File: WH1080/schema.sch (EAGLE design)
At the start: 18 parts

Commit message: +
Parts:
- removed ANEMO, RAIN: XRJK-S-01-6-4-0-9M2, con-xmultiple:XRJK-S-01-6-4-0-9M2
- added J1, J2: RJ11, SparkFun-Connectors:RJ11-6
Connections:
- net GND: now also J1.3, J2.2, J2.3; no longer ANEMO.1, ANEMO.2, RAIN.2
- net N$1: now also J1.4; no longer RAIN.3
- net N$2: now also J2.5; no longer ANEMO.4
- net N$4: now also J2.4; no longer ANEMO.3

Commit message: +
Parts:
- removed J1, J2: RJ11, SparkFun-Connectors:RJ11-6
- added RAIN, WIND: RJ11-4, pf:RJ11-4
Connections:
- net GND: now also RAIN.3, WIND.2, WIND.4; no longer J1.3, J2.2, J2.3
- net N$1: now also RAIN.4; no longer J1.4
- net N$2: now also WIND.5; no longer J2.5
- net N$4: now also WIND.3; no longer J2.4
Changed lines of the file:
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@@
 <grid distance="0.1" unitdist="inch" unit="inch" style="lines" multiple="1" display="no" altdistance="0.01" altunitdist="inch" altunit="inch"/>
 <layers>
-<layer number="1" name="Top" color="4" fill="1" visible="yes" active="no"/>
-<layer number="16" name="Bottom" color="1" fill="1" visible="yes" active="no"/>
-<layer number="17" name="Pads" color="2" fill="1" visible="yes" active="no"/>
-<layer number="18" name="Vias" color="2" fill="1" visible="yes" active="no"/>
-<layer number="19" name="Unrouted" color="6" fill="1" visible="yes" active="no"/>
-<layer number="20" name="Dimension" color="24" fill="1" visible="yes" active="no"/>
-<layer number="21" name="tPlace" color="7" fill="1" visible="yes" active="no"/>
-<layer number="22" name="bPlace" color="7" fill="1" visible="yes" active="no"/>
-<layer number="23" name="tOrigins" color="15" fill="1" visible="yes" active="no"/>
-<layer number="24" name="bOrigins" color="15" fill="1" visible="yes" active="no"/>
-<layer number="25" name="tNames" color="7" fill="1" visible="yes" active="no"/>
-<layer number="26" name="bNames" color="7" fill="1" visible="yes" active="no"/>
-<layer number="27" name="tValues" color="7" fill="1" visible="yes" active="no"/>
-<layer number="28" name="bValues" color="7" fill="1" visible="yes" active="no"/>
+<layer number="1" name="Top" color="4" fill="1" visible="no" active="no"/>
+<layer number="16" name="Bottom" color="1" fill="1" visible="no" active="no"/>
+<layer number="17" name="Pads" color="2" fill="1" visible="no" active="no"/>
+<layer number="18" name="Vias" color="2" fill="1" visible="no" active="no"/>
+<layer number="19" name="Unrouted" color="6" fill="1" visible="no" active="no"/>
+<layer number="20" name="Dimension" color="24" fill="1" visible="no" active="no"/>
+<layer number="21" name="tPlace" color="7" fill="1" visible="no" active="no"/>
+<layer number="22" name="bPlace" color="7" fill="1" visible="no" active="no"/>
+<layer number="23" name="tOrigins" color="15" fill="1" visible="no" active="no"/>
+<layer number="24" name="bOrigins" color="15" fill="1" visible="no" active="no"/>
+<layer number="25" name="tNames" color="7" fill="1" visible="no" active="no"/>
+<layer number="26" name="bNames" color="7" fill="1" visible="no" active="no"/>
+<layer number="27" name="tValues" color="7" fill="1" visible="no" active="no"/>
+<layer number="28" name="bValues" color="7" fill="1" visible="no" active="no"/>
 <layer number="29" name="tStop" color="7" fill="3" visible="no" active="no"/>
 <layer number="30" name="bStop" color="7" fill="6" visible="no" active="no"/>
@@
 <layer number="35" name="tGlue" color="7" fill="4" visible="no" active="no"/>
 <layer number="36" name="bGlue" color="7" fill="5" visible="no" active="no"/>
-<layer number="37" name="tTest" color="7" fill="1" visible="yes" active="no"/>
-<layer number="38" name="bTest" color="7" fill="1" visible="yes" active="no"/>
+<layer number="37" name="tTest" color="7" fill="1" visible="no" active="no"/>
+<layer number="38" name="bTest" color="7" fill="1" visible="no" active="no"/>
 <layer number="39" name="tKeepout" color="4" fill="11" visible="no" active="no"/>
 <layer number="40" name="bKeepout" color="1" fill="11" visible="no" active="no"/>
@@
 <layer number="44" name="Drills" color="7" fill="1" visible="no" active="no"/>
 <layer number="45" name="Holes" color="7" fill="1" visible="no" active="no"/>
-<layer number="46" name="Milling" color="3" fill="1" visible="yes" active="no"/>
-<layer number="47" name="Measures" color="7" fill="1" visible="yes" active="no"/>
-<layer number="48" name="Document" color="7" fill="1" visible="yes" active="no"/>
-<layer number="49" name="Reference" color="7" fill="1" visible="yes" active="no"/>
-<layer number="50" name="dxf" color="7" fill="1" visible="yes" active="no"/>
-<layer number="51" name="tDocu" color="7" fill="1" visible="yes" active="no"/>
-<layer number="52" name="bDocu" color="7" fill="1" visible="yes" active="no"/>
+<layer number="46" name="Milling" color="3" fill="1" visible="no" active="no"/>
+<layer number="47" name="Measures" color="7" fill="1" visible="no" active="no"/>
+<layer number="48" name="Document" color="7" fill="1" visible="no" active="no"/>
+<layer number="49" name="Reference" color="7" fill="1" visible="no" active="no"/>
+<layer number="50" name="dxf" color="7" fill="1" visible="no" active="no"/>
+<layer number="51" name="tDocu" color="7" fill="1" visible="no" active="no"/>
+<layer number="52" name="bDocu" color="7" fill="1" visible="no" active="no"/>
 <layer number="53" name="tGND_GNDA" color="7" fill="9" visible="no" active="no"/>
 <layer number="54" name="bGND_GNDA" color="1" fill="9" visible="no" active="no"/>
@@
 <part name="C3" library="rcl" library_urn="urn:adsk.eagle:library:334" deviceset="C-EU" device="025-024X044" package3d_urn="urn:adsk.eagle:package:23630/1" value="100n"/>
 <part name="GND9" library="supply1" library_urn="urn:adsk.eagle:library:371" deviceset="GND" device=""/>
-<part name="J1" library="SparkFun-Connectors" deviceset="RJ11-6" device="" value="RJ11"/>
-<part name="J2" library="SparkFun-Connectors" deviceset="RJ11-6" device="" value="RJ11"/>
+<part name="RAIN" library="pf" deviceset="RJ11-4" device=""/>
+<part name="WIND" library="pf" deviceset="RJ11-4" device=""/>
 </parts>
 <sheets>
@@
 <attribute name="VALUE" x="40.64" y="50.8" size="1.778" layer="96"/>
 </instance>
-<instance part="J1" gate="G$1" x="27.94" y="78.74" smashed="yes" rot="R180">
-<attribute name="VALUE" x="33.02" y="88.646" size="1.778" layer="96" font="vector" rot="R180"/>
-<attribute name="NAME" x="33.02" y="68.072" size="1.778" layer="95" font="vector" rot="R180"/>
-</instance>
-<instance part="J2" gate="G$1" x="66.04" y="81.28" smashed="yes" rot="R180">
-<attribute name="VALUE" x="71.12" y="91.186" size="1.778" layer="96" font="vector" rot="R180"/>
-<attribute name="NAME" x="71.12" y="70.612" size="1.778" layer="95" font="vector" rot="R180"/>
+<instance part="RAIN" gate="G$1" x="25.4" y="78.74" smashed="yes">
+<attribute name="NAME" x="22.86" y="83.82" size="1.778" layer="95"/>
+<attribute name="VALUE" x="22.86" y="70.612" size="1.778" layer="96"/>
+</instance>
+<instance part="WIND" gate="G$1" x="71.12" y="83.82" smashed="yes">
+<attribute name="NAME" x="68.58" y="88.9" size="1.778" layer="95"/>
+<attribute name="VALUE" x="68.58" y="75.692" size="1.778" layer="96"/>
 </instance>
 </instances>
@@
 <segment>
 <pinref part="GND5" gate="1" pin="GND"/>
-<wire x1="50.8" y1="78.74" x2="50.8" y2="81.28" width="0.1524" layer="91"/>
-<wire x1="50.8" y1="81.28" x2="50.8" y2="83.82" width="0.1524" layer="91"/>
-<wire x1="50.8" y1="83.82" x2="60.96" y2="83.82" width="0.1524" layer="91"/>
-<wire x1="60.96" y1="81.28" x2="50.8" y2="81.28" width="0.1524" layer="91"/>
-<junction x="50.8" y="81.28"/>
-<pinref part="J2" gate="G$1" pin="2"/>
-<pinref part="J2" gate="G$1" pin="3"/>
+<wire x1="50.8" y1="78.74" x2="50.8" y2="86.36" width="0.1524" layer="91"/>
+<pinref part="WIND" gate="G$1" pin="2"/>
+<wire x1="68.58" y1="86.36" x2="60.96" y2="86.36" width="0.1524" layer="91"/>
+<pinref part="WIND" gate="G$1" pin="4"/>
+<wire x1="60.96" y1="86.36" x2="50.8" y2="86.36" width="0.1524" layer="91"/>
+<wire x1="68.58" y1="81.28" x2="60.96" y2="81.28" width="0.1524" layer="91"/>
+<wire x1="60.96" y1="81.28" x2="60.96" y2="86.36" width="0.1524" layer="91"/>
+<junction x="60.96" y="86.36"/>
 </segment>
 <segment>
@@
 <pinref part="GND3" gate="1" pin="GND"/>
 <wire x1="5.08" y1="78.74" x2="5.08" y2="76.2" width="0.1524" layer="91"/>
+<pinref part="RAIN" gate="G$1" pin="3"/>
 <wire x1="22.86" y1="78.74" x2="5.08" y2="78.74" width="0.1524" layer="91"/>
-<pinref part="J1" gate="G$1" pin="3"/>
 </segment>
 </net>
@@
 <pinref part="WEMOS3" gate="D1" pin="D8"/>
 <wire x1="22.86" y1="33.02" x2="15.24" y2="33.02" width="0.1524" layer="91"/>
+<pinref part="RAIN" gate="G$1" pin="4"/>
 <wire x1="22.86" y1="76.2" x2="15.24" y2="76.2" width="0.1524" layer="91"/>
-<pinref part="J1" gate="G$1" pin="4"/>
 </segment>
 </net>
@@
 <wire x1="17.78" y1="45.72" x2="17.78" y2="63.5" width="0.1524" layer="91"/>
 <pinref part="WEMOS3" gate="D1" pin="A0"/>
-<wire x1="58.42" y1="76.2" x2="58.42" y2="63.5" width="0.1524" layer="91"/>
+<wire x1="58.42" y1="78.74" x2="58.42" y2="63.5" width="0.1524" layer="91"/>
 <wire x1="58.42" y1="63.5" x2="43.18" y2="63.5" width="0.1524" layer="91"/>
 <pinref part="R4" gate="G$1" pin="2"/>
@@
 <junction x="43.18" y="63.5"/>
 <pinref part="C3" gate="G$1" pin="1"/>
-<wire x1="60.96" y1="76.2" x2="58.42" y2="76.2" width="0.1524" layer="91"/>
-<pinref part="J2" gate="G$1" pin="5"/>
+<pinref part="WIND" gate="G$1" pin="5"/>
+<wire x1="68.58" y1="78.74" x2="58.42" y2="78.74" width="0.1524" layer="91"/>
 </segment>
 </net>
@@
 <junction x="50.8" y="60.96"/>
 <wire x1="20.32" y1="60.96" x2="50.8" y2="60.96" width="0.1524" layer="91"/>
-<wire x1="53.34" y1="60.96" x2="53.34" y2="78.74" width="0.1524" layer="91"/>
+<wire x1="53.34" y1="60.96" x2="53.34" y2="83.82" width="0.1524" layer="91"/>
 <junction x="53.34" y="60.96"/>
-<wire x1="53.34" y1="78.74" x2="60.96" y2="78.74" width="0.1524" layer="91"/>
-<pinref part="J2" gate="G$1" pin="4"/>
-</segment>
-</net>
+<pinref part="WIND" gate="G$1" pin="3"/>
+<wire x1="68.58" y1="83.82" x2="53.34" y2="83.82" width="0.1524" layer="91"/>
+</segment>
+</net>

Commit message: +
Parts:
- removed WEMOS3: (no value), esp8266modules:WEMOS-D1-MINI
- added R5: 4k7, rcl:R-EU_0204/7
- added U$1: WEMOS_S2_MINI, Wemos_Boards:WEMOS_S2_MINI
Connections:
- removed net +5V: WEMOS3.5V
- removed net N$3: CON->RAD.B-5, CON1.B-2, R1.1, WEMOS3.D4
- removed net N$5: CON->RAD.B-3, CON1.B-4, WEMOS3.D1
- removed net N$7: CON->RAD.B-4, CON1.B-3, WEMOS3.D2
- new net N$10: CON->MAIN.1, HUMIDITY.1, PRESSURE.1, SL3.1, SL4.1
- new net N$11: CON->MAIN.2, HUMIDITY.2, PRESSURE.2, SL3.2, SL4.2
- new net N$12: U$1.IO-39
- new net N$13: CON1.B-1, R1.2, U$1.IO-37
- new net N$14: CON->RAD.B-1, U$1.IO-16
- new net N$15: U$1.IO-12
- new net N$16: U$1.IO-11
- new net N$17: U$1.IO-9
- net +3V3: now also CON->RAD.B-2, CON1.B-2, R1.1, R5.1, U$1.3V3; no longer CON->RAD.B-1, CON1.B-6, R1.2, WEMOS3.3V3
- net GND: now also CON->RAD.B-3, CON1.B-3; no longer CON->RAD.B-6, CON1.B-1, WEMOS3.GND
- net N$1: now also U$1.IO-5; no longer WEMOS3.D8
- net N$2: now also U$1.IO-7; no longer WEMOS3.A0
- net N$4: now also U$1.IO-3; no longer WEMOS3.D7
- net N$9: now also R5.2
- net SCL: now also CON->RAD.B-5, CON1.B-5, U$1.IO-35/SCL; no longer CON->MAIN.2, HUMIDITY.2, PRESSURE.2, SL3.2, SL4.2
- net SDA: now also CON->RAD.B-4, CON1.B-4, U$1.IO-33/SDA; no longer CON->MAIN.1, HUMIDITY.1, PRESSURE.1, SL3.1, SL4.1
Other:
- note added: "Do CON->RAD"
- note added: "K půdnímu čidlu a čidlu osvitu"
- note added: "K čidlu srážek"
- note added: "K čidlu větru"
- moved on the sheet: R1

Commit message: vyroba DPS
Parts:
- added SL1: (no value), con-amp-quick:M02S
- added SL5: (no value), con-amp-quick:M04S
- U$1: value WEMOS_S2_MINI -> WEMOS-D1-MINI; device Wemos_Boards:WEMOS_S2_MINI -> Wemos_Boards:WEMOS-D1-MINI
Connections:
- removed net N$1: C1.1, R2.2, RAIN.4, U$1.IO-5
- removed net N$12: U$1.IO-39
- removed net N$15: U$1.IO-12
- removed net N$16: U$1.IO-11
- removed net N$17: U$1.IO-9
- removed net N$2: C3.1, R4.2, U$1.IO-7, WIND.5
- removed net N$4: C2.1, R3.2, U$1.IO-3, WIND.3
- new net GND1: CON->MAIN.3, HUMIDITY.3, PRESSURE.3, SL3.3, SL4.3, TEMPERATURE.GND
- new net PULS: C1.1, R2.2, RAIN.3, SL1-1.S, U$1.D8
- new net RYCHLOST: C2.1, R3.2, SL5-2.S, U$1.D7, WIND.3
- new net SMER: C3.1, R4.2, SL5-1.S, U$1.A0, WIND.4
- new net VCC: CON->MAIN.4, HUMIDITY.4, PRESSURE.4, R5.1, SL3.4, SL4.4, TEMPERATURE.VDD
- net +3V3: no longer CON->MAIN.4, HUMIDITY.4, PRESSURE.4, R5.1, SL3.4, SL4.4, TEMPERATURE.VDD
- net GND: now also RAIN.2, SL1-2.S, SL5-3.S, SL5-4.S, U$1.GND, WIND.1; no longer CON->MAIN.3, HUMIDITY.3, PRESSURE.3, RAIN.3, SL3.3, SL4.3, TEMPERATURE.GND, WIND.4
- net N$13: now also U$1.D3; no longer U$1.IO-37
- net N$14: now also U$1.D4; no longer U$1.IO-16
- net SCL: now also U$1.D1; no longer U$1.IO-35/SCL
- net SDA: now also U$1.D2; no longer U$1.IO-33/SDA

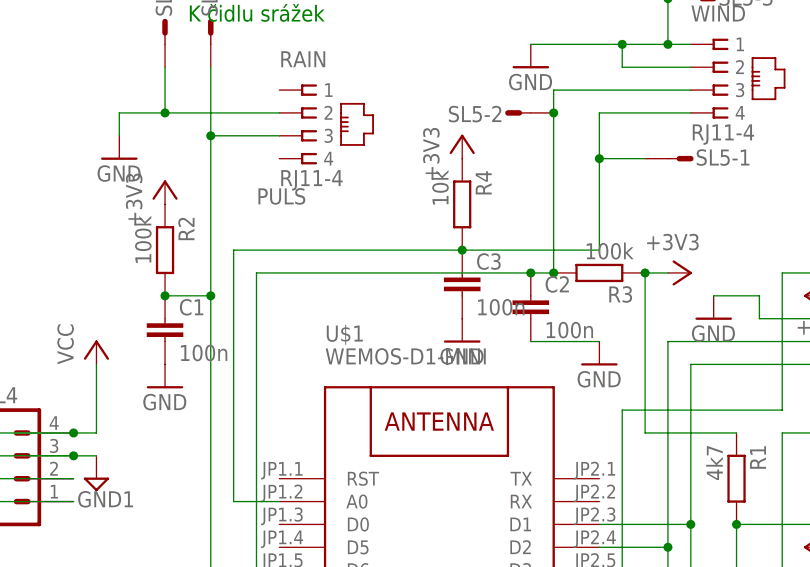
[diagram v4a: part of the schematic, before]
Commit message: změna odporu pro dělič směru větru
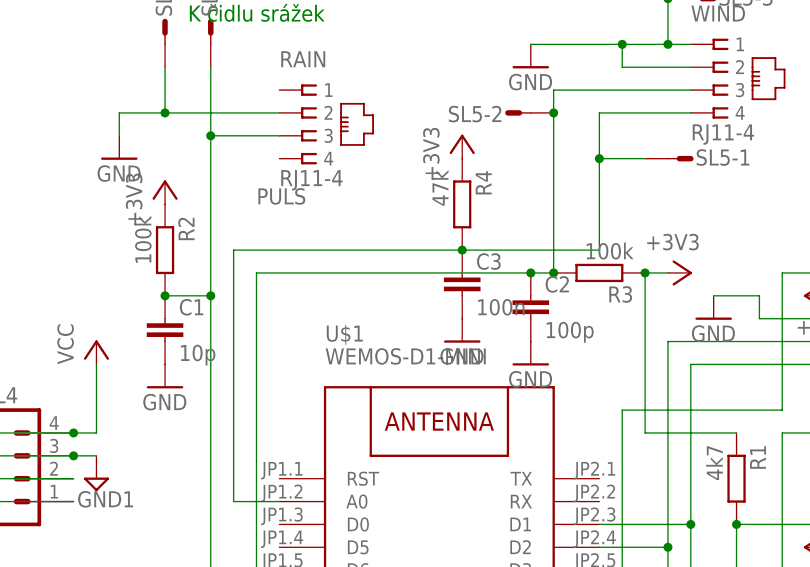
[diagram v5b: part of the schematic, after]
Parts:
- C1: value 100n -> 10p
- C2: value 100n -> 100p
- R4: value 10k -> 47k
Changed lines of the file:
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@@
 <part name="R2" library="rcl" library_urn="urn:adsk.eagle:library:334" deviceset="R-EU_" device="0204/7" package3d_urn="urn:adsk.eagle:package:23498/2" value="100k"/>
 <part name="+3V2" library="supply1" library_urn="urn:adsk.eagle:library:371" deviceset="+3V3" device=""/>
-<part name="C1" library="rcl" library_urn="urn:adsk.eagle:library:334" deviceset="C-EU" device="025-024X044" package3d_urn="urn:adsk.eagle:package:23630/1" value="100n"/>
+<part name="C1" library="rcl" library_urn="urn:adsk.eagle:library:334" deviceset="C-EU" device="025-024X044" package3d_urn="urn:adsk.eagle:package:23630/1" value="10p"/>
 <part name="GND4" library="supply1" library_urn="urn:adsk.eagle:library:371" deviceset="GND" device=""/>
 <part name="GND5" library="supply1" library_urn="urn:adsk.eagle:library:371" deviceset="GND" device=""/>
 <part name="R3" library="rcl" library_urn="urn:adsk.eagle:library:334" deviceset="R-EU_" device="0204/7" package3d_urn="urn:adsk.eagle:package:23498/2" value="100k"/>
 <part name="+3V3" library="supply1" library_urn="urn:adsk.eagle:library:371" deviceset="+3V3" device=""/>
-<part name="C2" library="rcl" library_urn="urn:adsk.eagle:library:334" deviceset="C-EU" device="025-024X044" package3d_urn="urn:adsk.eagle:package:23630/1" value="100n"/>
+<part name="C2" library="rcl" library_urn="urn:adsk.eagle:library:334" deviceset="C-EU" device="025-024X044" package3d_urn="urn:adsk.eagle:package:23630/1" value="100p"/>
 <part name="GND6" library="supply1" library_urn="urn:adsk.eagle:library:371" deviceset="GND" device=""/>
 <part name="CON-&gt;RAD" library="con-wago" library_urn="urn:adsk.eagle:library:197" deviceset="233-506" device="" package3d_urn="urn:adsk.eagle:package:8079516/1"/>
@@
 <part name="TEMPERATURE" library="DS1820" deviceset="DS1820" device=""/>
 <part name="CON-&gt;MAIN" library="con-amp-quick" library_urn="urn:adsk.eagle:library:125" deviceset="M05" device="" package3d_urn="urn:adsk.eagle:package:5961/1"/>
-<part name="R4" library="rcl" library_urn="urn:adsk.eagle:library:334" deviceset="R-EU_" device="0204/7" package3d_urn="urn:adsk.eagle:package:23498/2" value="10k"/>
+<part name="R4" library="rcl" library_urn="urn:adsk.eagle:library:334" deviceset="R-EU_" device="0204/7" package3d_urn="urn:adsk.eagle:package:23498/2" value="47k"/>
 <part name="+3V7" library="supply1" library_urn="urn:adsk.eagle:library:371" deviceset="+3V3" device=""/>
 <part name="C3" library="rcl" library_urn="urn:adsk.eagle:library:334" deviceset="C-EU" device="025-024X044" package3d_urn="urn:adsk.eagle:package:23630/1" value="100n"/>
@@
 <attribute name="VALUE" x="52.324" y="53.721" size="1.778" layer="96"/>
 </instance>
-<instance part="GND6" gate="1" x="58.42" y="50.8" smashed="yes">
-<attribute name="VALUE" x="55.88" y="48.26" size="1.778" layer="96"/>
+<instance part="GND6" gate="1" x="50.8" y="50.8" smashed="yes">
+<attribute name="VALUE" x="48.26" y="48.26" size="1.778" layer="96"/>
 </instance>
 <instance part="CON-&gt;RAD" gate="G$1" x="91.44" y="55.88" smashed="yes">
@@
 <pinref part="C2" gate="G$1" pin="2"/>
 <pinref part="GND6" gate="1" pin="GND"/>
-<wire x1="50.8" y1="53.34" x2="58.42" y2="53.34" width="0.1524" layer="91"/>
-</segment>
-<segment>
+</segment>
+<segment>

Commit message: +
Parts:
- R2: value 100k -> 10k
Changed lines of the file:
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@@
 <parts>
 <part name="GND3" library="supply1" library_urn="urn:adsk.eagle:library:371" deviceset="GND" device=""/>
-<part name="R2" library="rcl" library_urn="urn:adsk.eagle:library:334" deviceset="R-EU_" device="0204/7" package3d_urn="urn:adsk.eagle:package:23498/2" value="100k"/>
+<part name="R2" library="rcl" library_urn="urn:adsk.eagle:library:334" deviceset="R-EU_" device="0204/7" package3d_urn="urn:adsk.eagle:package:23498/2" value="10k"/>
 <part name="+3V2" library="supply1" library_urn="urn:adsk.eagle:library:371" deviceset="+3V3" device=""/>
 <part name="C1" library="rcl" library_urn="urn:adsk.eagle:library:334" deviceset="C-EU" device="025-024X044" package3d_urn="urn:adsk.eagle:package:23630/1" value="10p"/>
